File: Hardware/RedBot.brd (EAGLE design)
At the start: 94 x 49.5 mm, 62 parts, among them U1 ATMEGA328P, U2 TB6612FNG, U3 MIC5219 5V, U4 MIC5219 3.3V, U5 FT232RLSSOP, Y1 16MHz

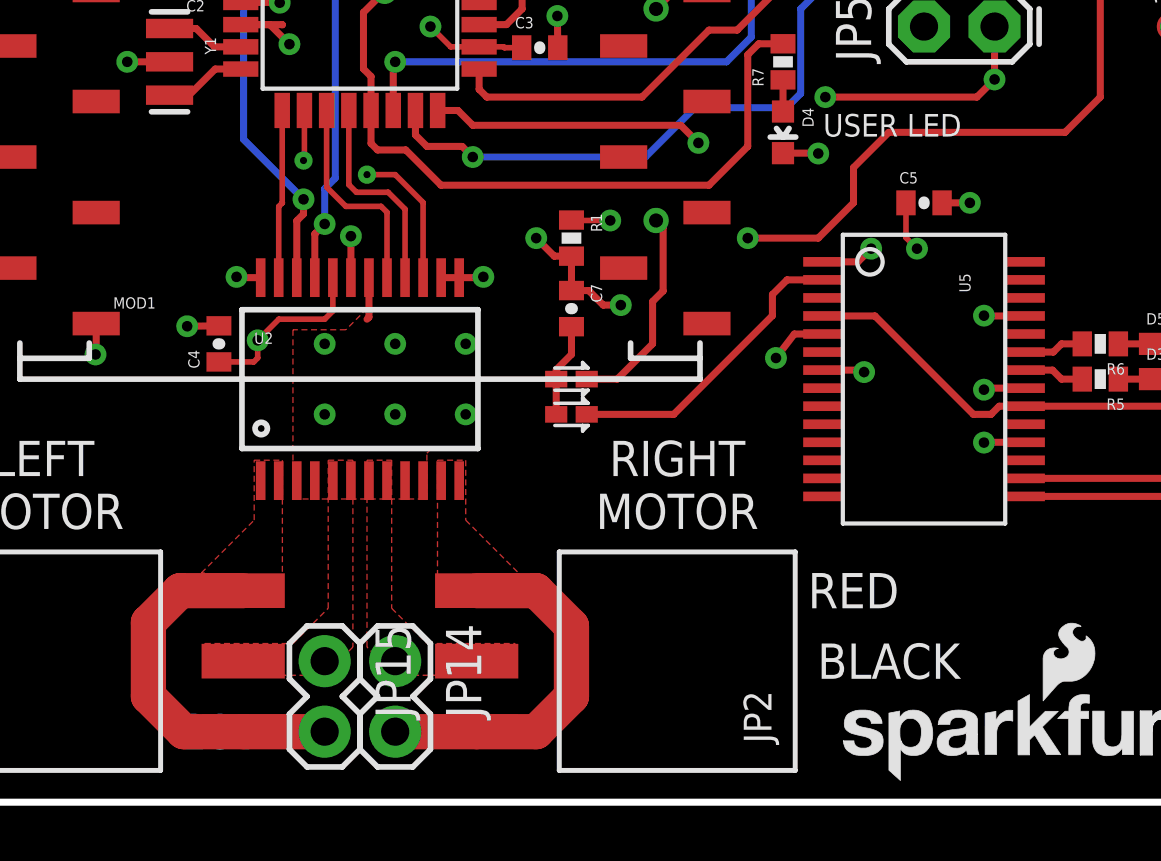
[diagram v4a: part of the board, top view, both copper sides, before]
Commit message: Fix a couple of problems: - TEST pin on FTDI chip needs to be grounded. - FTDI chip not properly bypassed.
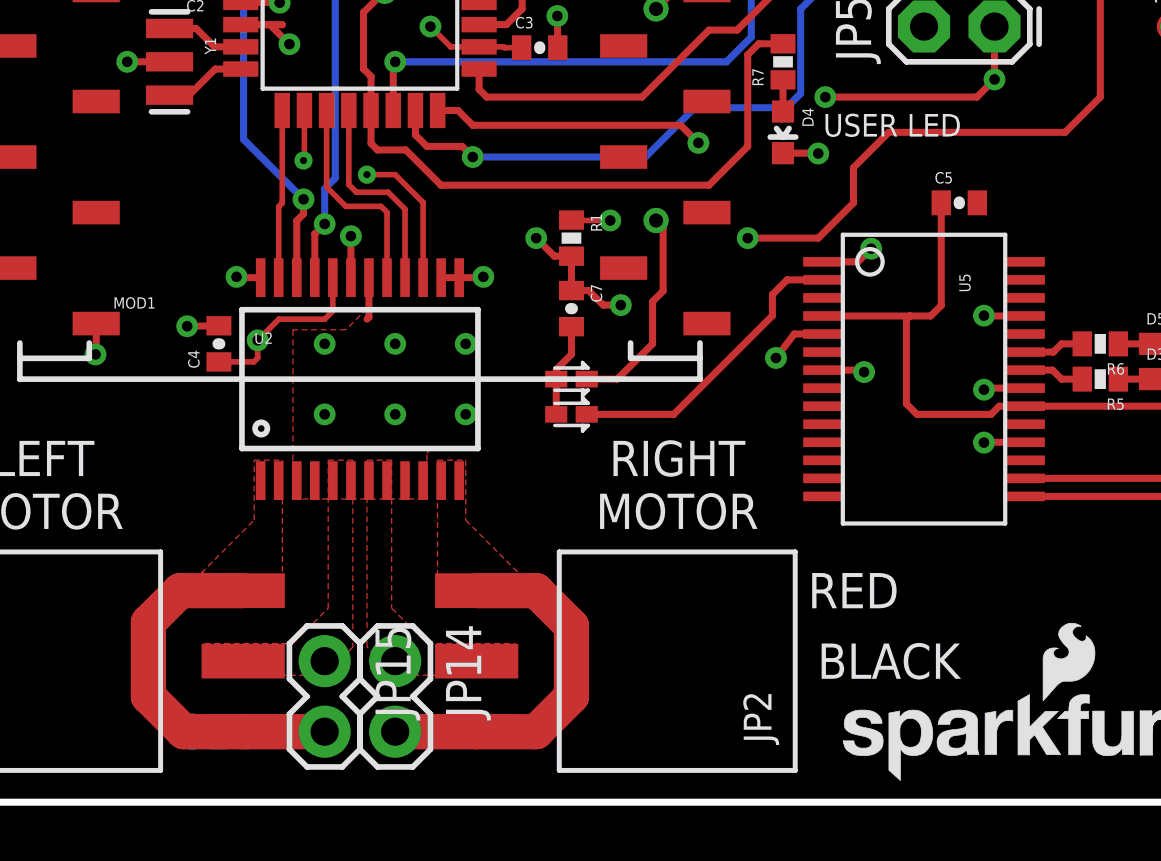
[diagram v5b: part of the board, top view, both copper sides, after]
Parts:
- moved C5 1.27 mm to (68.6, 21.6)
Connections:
- net 5V: no longer C5.1
- net GND: now also U5.26
- net V_USB: now also C5.1
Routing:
- net V_USB: track 36.5 -> 43.5 mm
- net 5V: track 59.2 -> 57.4 mm, vias 19 -> 18
- net GND: track 84.5 -> 83.5 mm, vias 45 -> 44
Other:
- board text added: "v10"
- board text removed: "v02"
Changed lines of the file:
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@@
 <layer number="1" name="Top" color="4" fill="1" visible="no" active="yes"/>
 <layer number="2" name="5V" color="1" fill="3" visible="no" active="yes"/>
-<layer number="15" name="Gnd" color="4" fill="6" visible="yes" active="yes"/>
-<layer number="16" name="Bottom" color="1" fill="1" visible="no" active="yes"/>
+<layer number="15" name="Gnd" color="4" fill="6" visible="no" active="yes"/>
+<layer number="16" name="Bottom" color="1" fill="1" visible="yes" active="yes"/>
 <layer number="17" name="Pads" color="2" fill="1" visible="no" active="yes"/>
 <layer number="18" name="Vias" color="2" fill="1" visible="yes" active="yes"/>
@@
 <layer number="46" name="Milling" color="3" fill="1" visible="no" active="yes"/>
 <layer number="51" name="tDocu" color="6" fill="1" visible="no" active="yes"/>
+<layer number="52" name="bDocu" color="7" fill="1" visible="no" active="yes"/>
 <layer number="3" name="Route3" color="4" fill="3" visible="no" active="no"/>
 <layer number="4" name="Route4" color="1" fill="4" visible="no" active="no"/>
@@
 <layer number="49" name="Reference" color="7" fill="1" visible="no" active="no"/>
 <layer number="50" name="dxf" color="7" fill="1" visible="no" active="no"/>
-<layer number="52" name="bDocu" color="7" fill="1" visible="no" active="no"/>
 <layer number="53" name="tGND_GNDA" color="7" fill="9" visible="no" active="no"/>
 <layer number="54" name="bGND_GNDA" color="1" fill="9" visible="no" active="no"/>
@@
 <text x="58.42" y="44.323" size="1.27" layer="21" font="vector" ratio="15" align="center">POWER</text>
 <text x="66.167" y="24.384" size="0.8128" layer="21" font="vector" ratio="15" align="center">USER LED</text>
-<text x="41.91" y="2.54" size="1.27" layer="16" font="vector" ratio="15" rot="MR0" align="center">v02</text>
+<text x="41.91" y="2.54" size="1.27" layer="16" font="vector" ratio="15" rot="MR0" align="center">v10</text>
 <text x="3.175" y="41.021" size="0.8128" layer="21" font="vector" ratio="15">5V</text>
 <text x="7.493" y="38.989" size="0.8128" layer="21" font="vector" ratio="15">GND</text>
@@
 <attribute name="VALUE" value="0.1uF" x="114.3" y="78.74" size="1.778" layer="27" rot="R90" display="off"/>
 </element>
-<element name="C5" library="SparkFun-Capacitors" package="0402-CAP" value="0.1uF" x="67.31" y="21.59">
-<attribute name="PROD_ID" value="CAP-00810" x="133.35" y="-50.8" size="1.778" layer="27" display="off"/>
-<attribute name="VALUE" value="0.1uF" x="133.35" y="-50.8" size="1.778" layer="27" display="off"/>
+<element name="C5" library="SparkFun-Capacitors" package="0402-CAP" value="0.1uF" x="68.58" y="21.59">
+<attribute name="PROD_ID" value="CAP-00810" x="134.62" y="-50.8" size="1.778" layer="27" display="off"/>
+<attribute name="VALUE" value="0.1uF" x="134.62" y="-50.8" size="1.778" layer="27" display="off"/>
 </element>
 <element name="C6" library="SparkFun-Capacitors" package="0402-CAP" value="0.1uF" x="36.068" y="37.719">
@@
 <contactref element="C3" pad="2"/>
 <contactref element="C4" pad="2"/>
-<contactref element="C5" pad="2"/>
 <polygon width="0.254" layer="15" isolate="0.3048">
 <vertex x="2.54" y="49.53"/>
@@
 <wire x1="76.95" y1="17.387" x2="76.962" y2="17.526" width="0.254" layer="1"/>
 <via x="76.962" y="17.526" extent="1-16" drill="0.381"/>
-<wire x1="67.96" y1="21.59" x2="68.961" y2="21.59" width="0.254" layer="1"/>
-<via x="68.961" y="21.59" extent="1-16" drill="0.381"/>
 <wire x1="70.966" y1="17.515" x2="69.48" y2="17.515" width="0.254" layer="1"/>
 <wire x1="69.48" y1="17.515" x2="69.469" y2="17.526" width="0.254" layer="1"/>
@@
 <vertex x="0" y="46.99" curve="-90"/>
 </polygon>
+<contactref element="C5" pad="2"/>
+<contactref element="U5" pad="26"/>
 </signal>
 <signal name="SENSOR_0/SW_TXO">
@@
 <contactref element="C3" pad="1"/>
 <contactref element="C4" pad="1"/>
-<contactref element="C5" pad="1"/>
 <wire x1="41.163" y1="29.591" x2="42.6784" y2="29.591" width="0.254" layer="1"/>
 <wire x1="42.6784" y1="29.591" x2="42.6974" y2="29.61" width="0.254" layer="1"/>
@@
 <wire x1="78.74" y1="30.48" x2="76.2" y2="30.48" width="0.2032" layer="1"/>
 <wire x1="83.82" y1="30.48" x2="86.36" y2="30.48" width="0.2032" layer="1"/>
-<wire x1="66.66" y1="21.59" x2="66.66" y2="20.335" width="0.2032" layer="1"/>
-<wire x1="66.66" y1="20.335" x2="67.056" y2="19.939" width="0.2032" layer="1"/>
-<via x="67.056" y="19.939" extent="1-16" drill="0.381"/>
 <wire x1="46.015" y1="18.896" x2="46.015" y2="17.694" width="0.2032" layer="1"/>
 <wire x1="46.015" y1="17.694" x2="45.72" y2="17.399" width="0.2032" layer="1"/>
@@
 <wire x1="70.966" y1="14.265" x2="70.018" y2="14.265" width="0.254" layer="1"/>
 <wire x1="70.018" y1="14.265" x2="69.723" y2="13.97" width="0.254" layer="1"/>
-<wire x1="69.723" y1="13.97" x2="69.088" y2="13.97" width="0.254" layer="1"/>
-<wire x1="69.088" y1="13.97" x2="65.543" y2="17.515" width="0.254" layer="1"/>
-<wire x1="63.654" y1="17.515" x2="65.543" y2="17.515" width="0.254" layer="1"/>
 <wire x1="79.289" y1="14.265" x2="79.883" y2="14.859" width="0.254" layer="1"/>
 <via x="79.883" y="14.859" extent="1-16" drill="0.508"/>
@@
 <wire x1="87.757" y1="8.763" x2="88.51" y2="8.01" width="0.8128" layer="1"/>
 <wire x1="88.51" y1="6.35" x2="88.51" y2="8.01" width="0.8128" layer="1"/>
+<contactref element="C5" pad="1"/>
+<wire x1="63.654" y1="17.515" x2="66.802" y2="17.515" width="0.254" layer="1"/>
+<wire x1="66.802" y1="17.515" x2="67.553" y2="17.515" width="0.254" layer="1"/>
+<wire x1="67.553" y1="17.515" x2="67.93" y2="17.892" width="0.254" layer="1"/>
+<wire x1="67.93" y1="21.59" x2="67.93" y2="17.892" width="0.254" layer="1"/>
+<wire x1="69.723" y1="13.97" x2="67.056" y2="13.97" width="0.254" layer="1"/>
+<wire x1="67.056" y1="13.97" x2="66.675" y2="14.351" width="0.254" layer="1"/>
+<wire x1="66.675" y1="14.351" x2="66.675" y2="17.388" width="0.254" layer="1"/>
+<wire x1="66.675" y1="17.388" x2="66.802" y2="17.515" width="0.254" layer="1"/>
 </signal>
 <signal name="PROGRAM_ENABLE">
@@
 </signal>
 </signals>
-<errors>
-</errors>
 </board>
 </drawing>

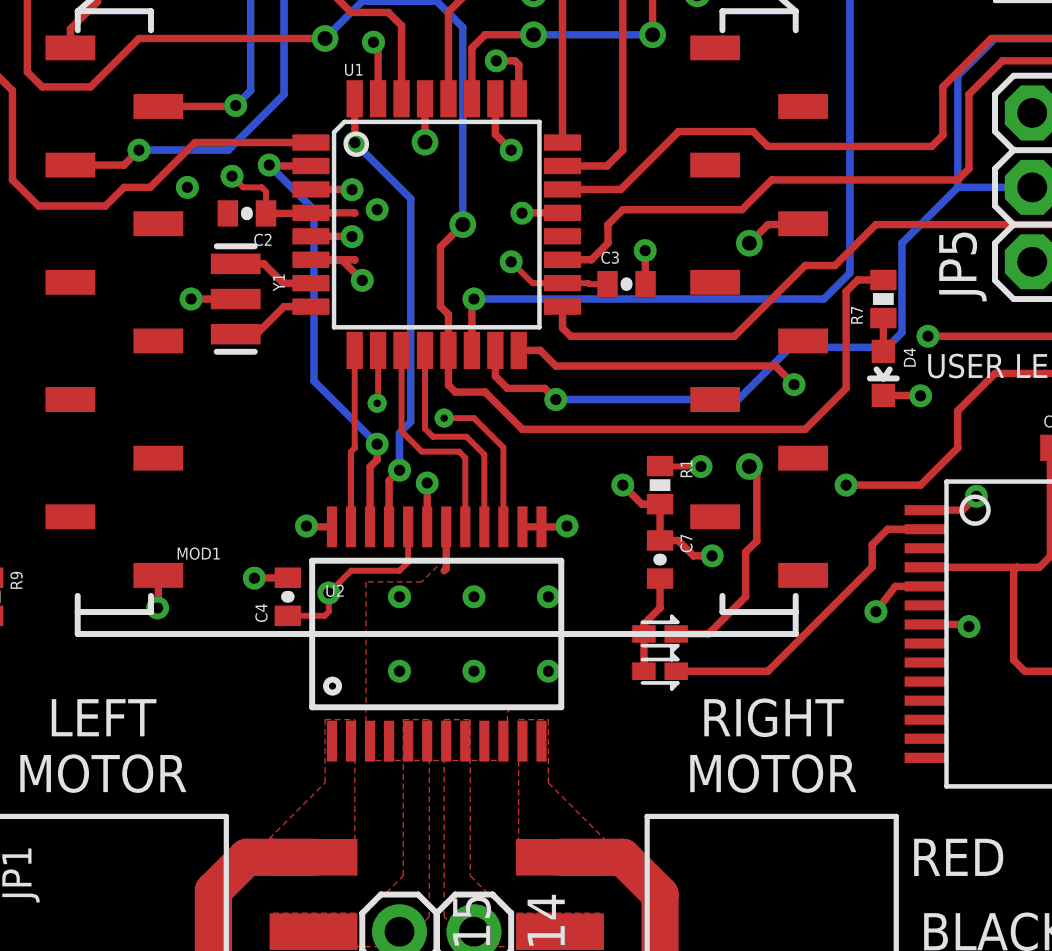
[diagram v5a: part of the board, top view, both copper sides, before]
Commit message: Added an AND gate to the reset lines, to improve the multiplexing capabilities of the Xbee/FTDI during bootloads.
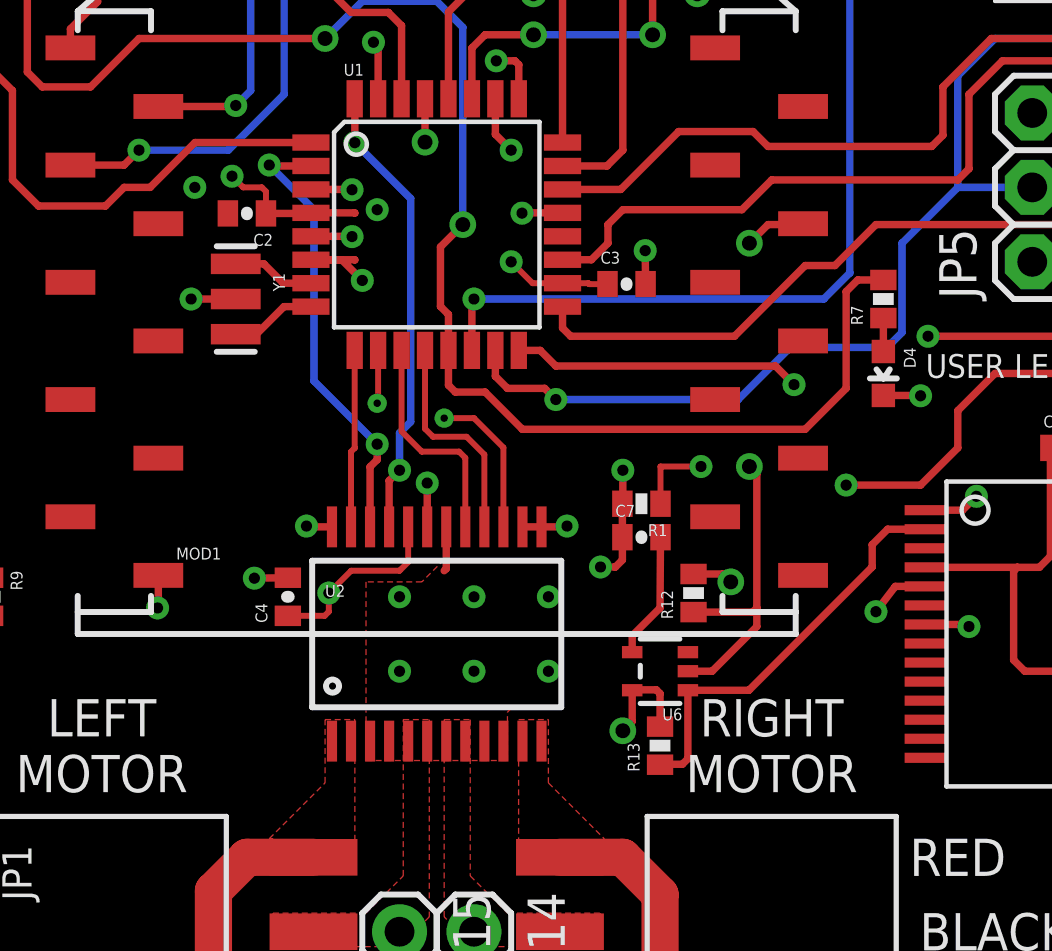
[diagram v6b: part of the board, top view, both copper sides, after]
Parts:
- removed D7, D8: RB751, SparkFun-DiscreteSemi:SOD-523
- added R12, R13: 10k, SparkFun-Resistors:0402-RES
- added U6: 7408SE, SparkFun-DigitalIC:SOT353
- moved C7 0.99 mm to (54.0, 18.5), turned to 0 degrees
- moved R1 0.90 mm to (54.0, 19.7), turned to 180 degrees
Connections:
- net 5V: now also R12.2, R13.2, U6.5
- net FTDI_DTR: now also R13.1, U6.1; no longer D8.C
- net GND: now also U6.3
- net N$5: now also U6.4; no longer D7.A, D8.A
- net XBEE_DIO3: now also R12.1, U6.2; no longer D7.C
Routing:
- net 5V: track 57.4 -> 63.7 mm, vias 18 -> 20
- net FTDI_DTR: track 10.9 -> 14.2 mm
- net XBEE_DIO3: track 17.6 -> 20.8 mm
- net RESET: track 81.5 -> 84.1 mm
- net N$5: track 3.39 -> 4.32 mm
